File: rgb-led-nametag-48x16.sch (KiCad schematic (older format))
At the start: 25 parts, among them J1 USB_C_Receptacle_USB2.0, J2 TagConnect_TC2030_SWD, U25 STM32F722RETx, U26 SRV05-4, U27 TPS63001

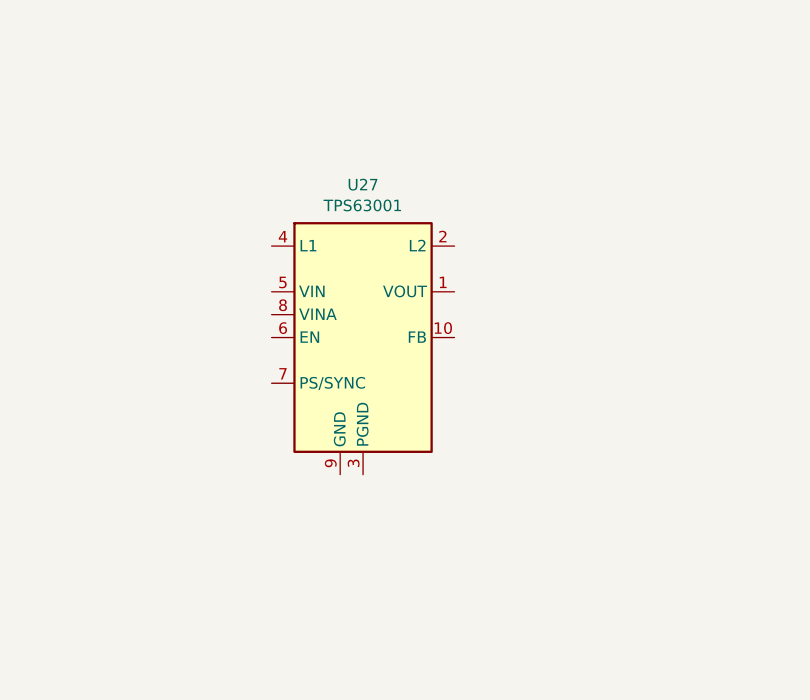
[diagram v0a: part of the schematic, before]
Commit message: Layout 3V3 buck/boost converter
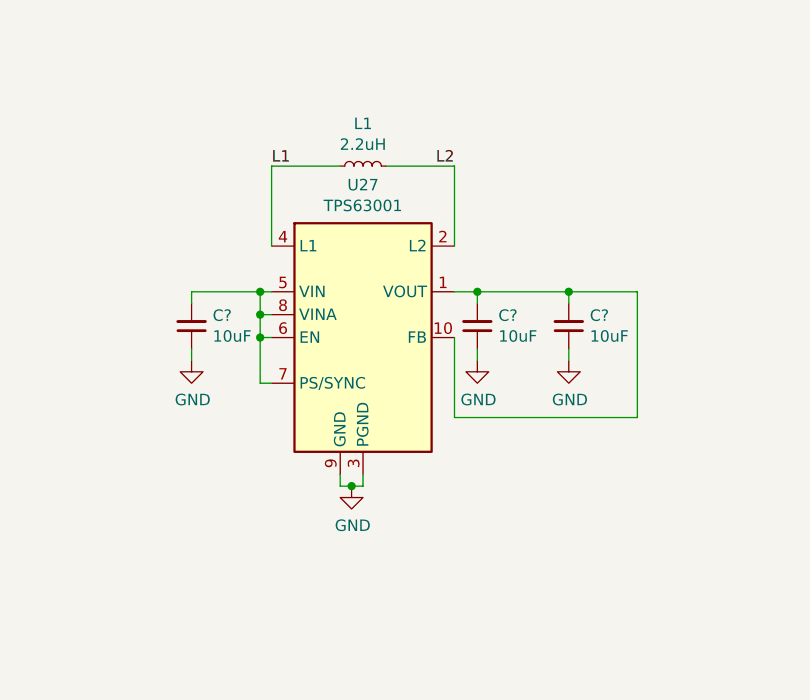
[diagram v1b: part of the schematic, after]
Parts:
- added C? (x3): 10uF, Capacitor_SMD:C_0402_1005Metric, symbol Device:C_Small
- added L1: 2.2uH, Inductor_SMD:L_Taiyo-Yuden_MD-3030, symbol Device:L_Small
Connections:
- net GND: now also U27.11 (PGND), U27.3 (PGND), U27.9 (GND), C?.1, C?.1, C?.1
- net at U27.1 (VOUT): now also U27.10 (FB), C?.2, C?.2
- net L2: now reaches U27.2 (L2)
- net L2: now also L1.2
- net L1: now reaches U27.4 (L1)
- net L1: now also L1.1
- net at U27.5 (VIN): now also U27.6 (EN), U27.7 (PS/SYNC), U27.8 (VINA), C?.2
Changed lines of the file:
@@
 	1550 4550 1550 4500
 Connection ~ 1550 4500
+$Comp
+L Device:L_Small L1
+U 1 1 623B26A7
+P 12600 1150
+F 0 "L1" V 12785 1150 50  0000 C CNN
+F 1 "2.2uH" V 12694 1150 50  0000 C CNN
+F 2 "Inductor_SMD:L_Taiyo-Yuden_MD-3030" H 12600 1150 50  0001 C CNN
+F 3 "~" H 12600 1150 50  0001 C CNN
+F 4 "C43389" V 12600 1150 50  0001 C CNN "LCSC"
+	1    12600 1150
+	0    -1   -1   0
+$EndComp
+Wire Wire Line
+	12500 1150 12200 1150
+Wire Wire Line
+	12200 1150 12200 1500
+Wire Wire Line
+	12700 1150 13000 1150
+Wire Wire Line
+	13000 1150 13000 1500
+Text Label 12200 1150 0    50   ~ 0
+L1
+Text Label 13000 1150 2    50   ~ 0
+L2
+$Comp
+L Device:C_Small C?
+U 1 1 623DDBAB
+P 11850 1850
+AR Path="/620161BA/623DDBAB" Ref="C?"  Part="1"
+AR Path="/623DDBAB" Ref="C?"  Part="1"
+F 0 "C?" H 11758 1804 50  0000 R CNN
+F 1 "10uF" H 11758 1895 50  0000 R CNN
+F 2 "Capacitor_SMD:C_0402_1005Metric" H 11850 1850 50  0001 C CNN
+F 3 "~" H 11850 1850 50  0001 C CNN
+F 4 "C15525" H 11850 1850 50  0001 C CNN "LCSC"
+	1    11850 1850
+	-1   0    0    1
+$EndComp
+Wire Wire Line
+	12200 1700 12150 1700
+Wire Wire Line
+	11850 1700 11850 1750
+Wire Wire Line
+	12200 1800 12150 1800
+Wire Wire Line
+	12150 1800 12150 1700
+Connection ~ 12150 1700
+Wire Wire Line
+	12150 1700 11850 1700
+Wire Wire Line
+	12200 1900 12150 1900
+Wire Wire Line
+	12150 1900 12150 1800
+Connection ~ 12150 1800
+Wire Wire Line
+	12200 2100 12150 2100
+Wire Wire Line
+	12150 2100 12150 1900
+Connection ~ 12150 1900
+$Comp
+L power:GND #PWR?
+U 1 1 6241DC69
+P 11850 2000
+F 0 "#PWR?" H 11850 1750 50  0001 C CNN
+F 1 "GND" H 11855 1827 50  0000 C CNN
+F 2 "" H 11850 2000 50  0001 C CNN
+F 3 "" H 11850 2000 50  0001 C CNN
+	1    11850 2000
+	1    0    0    -1
+$EndComp
+Wire Wire Line
+	11850 2000 11850 1950
+$Comp
+L power:GND #PWR?
+U 1 1 6242BAF6
+P 12550 2550
+F 0 "#PWR?" H 12550 2300 50  0001 C CNN
+F 1 "GND" H 12555 2377 50  0000 C CNN
+F 2 "" H 12550 2550 50  0001 C CNN
+F 3 "" H 12550 2550 50  0001 C CNN
+	1    12550 2550
+	1    0    0    -1
+$EndComp
+Wire Wire Line
+	12500 2500 12500 2550
+Wire Wire Line
+	12500 2550 12550 2550
+Wire Wire Line
+	12600 2500 12600 2550
+Wire Wire Line
+	12600 2550 12550 2550
+Connection ~ 12550 2550
+$Comp
+L Device:C_Small C?
+U 1 1 62448BCD
+P 13100 1850
+AR Path="/620161BA/62448BCD" Ref="C?"  Part="1"
+AR Path="/62448BCD" Ref="C?"  Part="1"
+F 0 "C?" H 13008 1804 50  0000 R CNN
+F 1 "10uF" H 13008 1895 50  0000 R CNN
+F 2 "Capacitor_SMD:C_0402_1005Metric" H 13100 1850 50  0001 C CNN
+F 3 "~" H 13100 1850 50  0001 C CNN
+F 4 "C15525" H 13100 1850 50  0001 C CNN "LCSC"
+	1    13100 1850
+	-1   0    0    1
+$EndComp
+$Comp
+L Device:C_Small C?
+U 1 1 6245675E
+P 13500 1850
+AR Path="/620161BA/6245675E" Ref="C?"  Part="1"
+AR Path="/6245675E" Ref="C?"  Part="1"
+F 0 "C?" H 13408 1804 50  0000 R CNN
+F 1 "10uF" H 13408 1895 50  0000 R CNN
+F 2 "Capacitor_SMD:C_0402_1005Metric" H 13500 1850 50  0001 C CNN
+F 3 "~" H 13500 1850 50  0001 C CNN
+F 4 "C15525" H 13500 1850 50  0001 C CNN "LCSC"
+	1    13500 1850
+	-1   0    0    1
+$EndComp
+Wire Wire Line
+	13000 1700 13100 1700
+Wire Wire Line
+	13500 1700 13500 1750
+Wire Wire Line
+	13100 1750 13100 1700
+Connection ~ 13100 1700
+Wire Wire Line
+	13100 1700 13500 1700
+$Comp
+L power:GND #PWR?
+U 1 1 6247F801
+P 13100 2000
+F 0 "#PWR?" H 13100 1750 50  0001 C CNN
+F 1 "GND" H 13105 1827 50  0000 C CNN
+F 2 "" H 13100 2000 50  0001 C CNN
+F 3 "" H 13100 2000 50  0001 C CNN
+	1    13100 2000
+	1    0    0    -1
+$EndComp
+Wire Wire Line
+	13100 2000 13100 1950
+$Comp
+L power:GND #PWR?
+U 1 1 6248E1C3
+P 13500 2000
+F 0 "#PWR?" H 13500 1750 50  0001 C CNN
+F 1 "GND" H 13505 1827 50  0000 C CNN
+F 2 "" H 13500 2000 50  0001 C CNN
+F 3 "" H 13500 2000 50  0001 C CNN
+	1    13500 2000
+	1    0    0    -1
+$EndComp
+Wire Wire Line
+	13500 2000 13500 1950
+Wire Wire Line
+	13000 1900 13000 2250
+Wire Wire Line
+	13000 2250 13800 2250
+Wire Wire Line
+	13800 2250 13800 1700
+Wire Wire Line
+	13800 1700 13500 1700
 Wire Bus Line
 	2950 1250 2950 6650
+Connection ~ 13500 1700
 $EndSCHEMATC

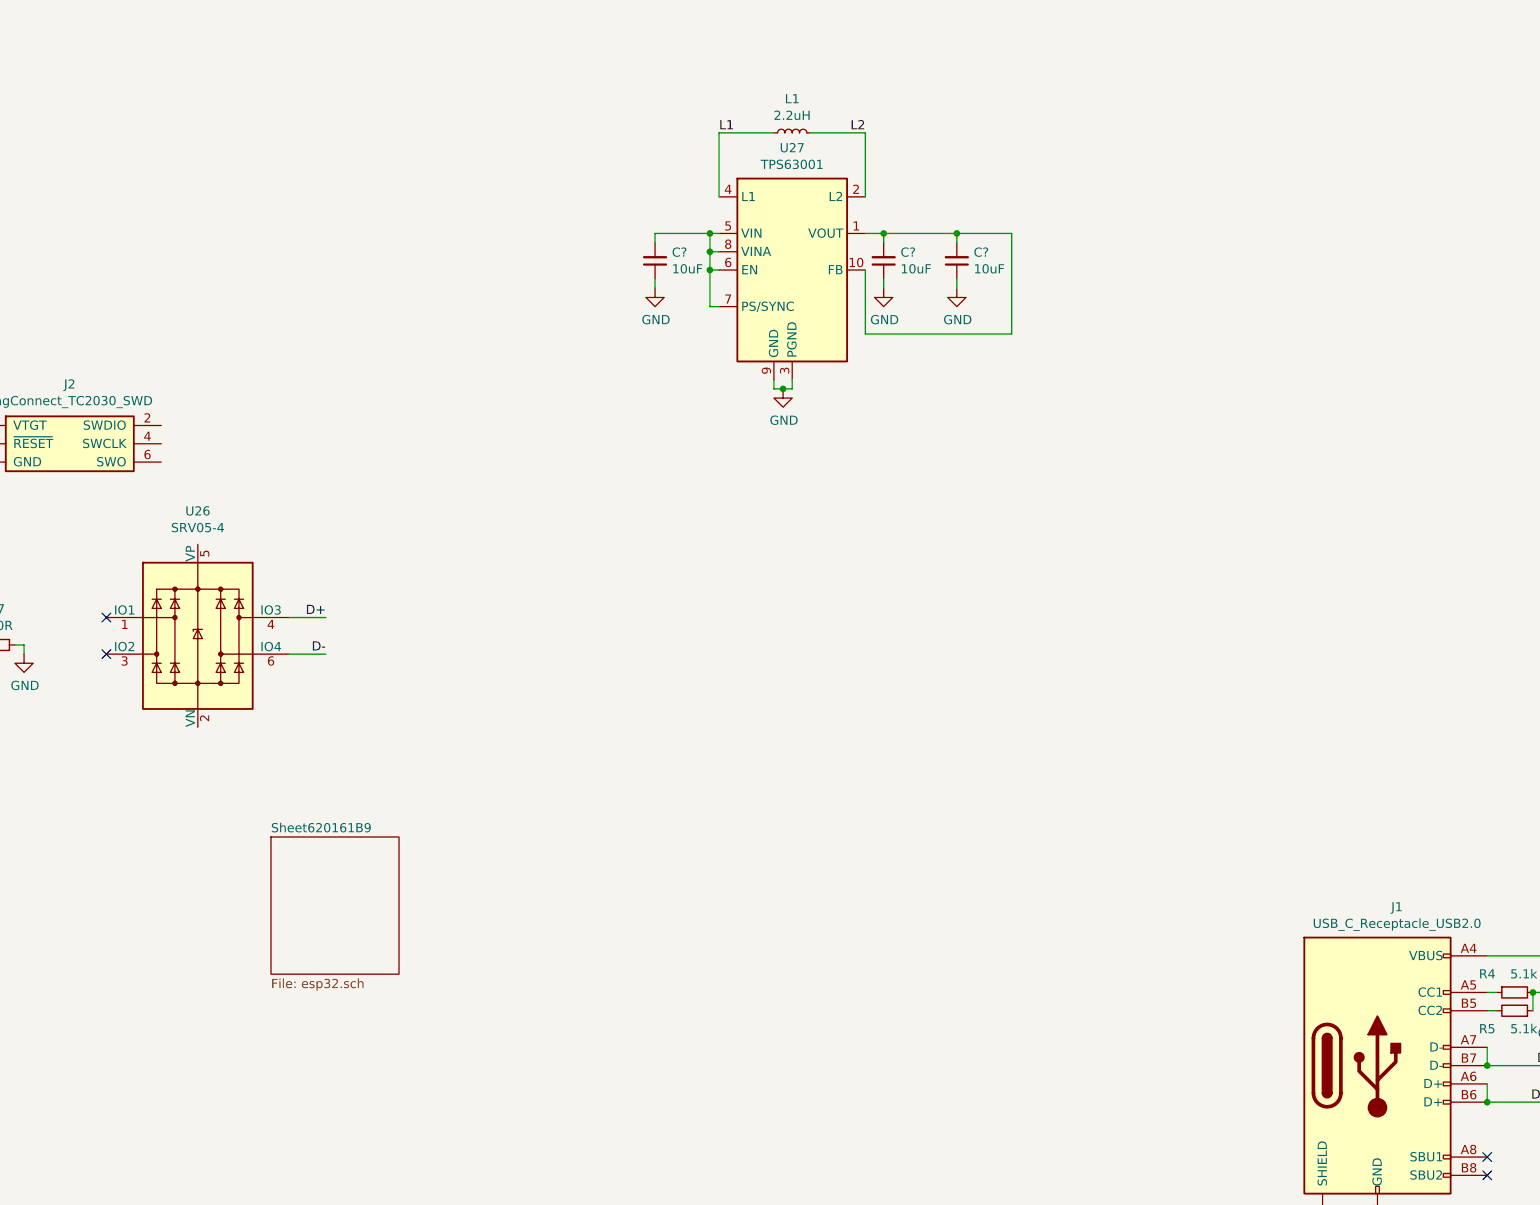
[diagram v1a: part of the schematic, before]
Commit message: Implement power path
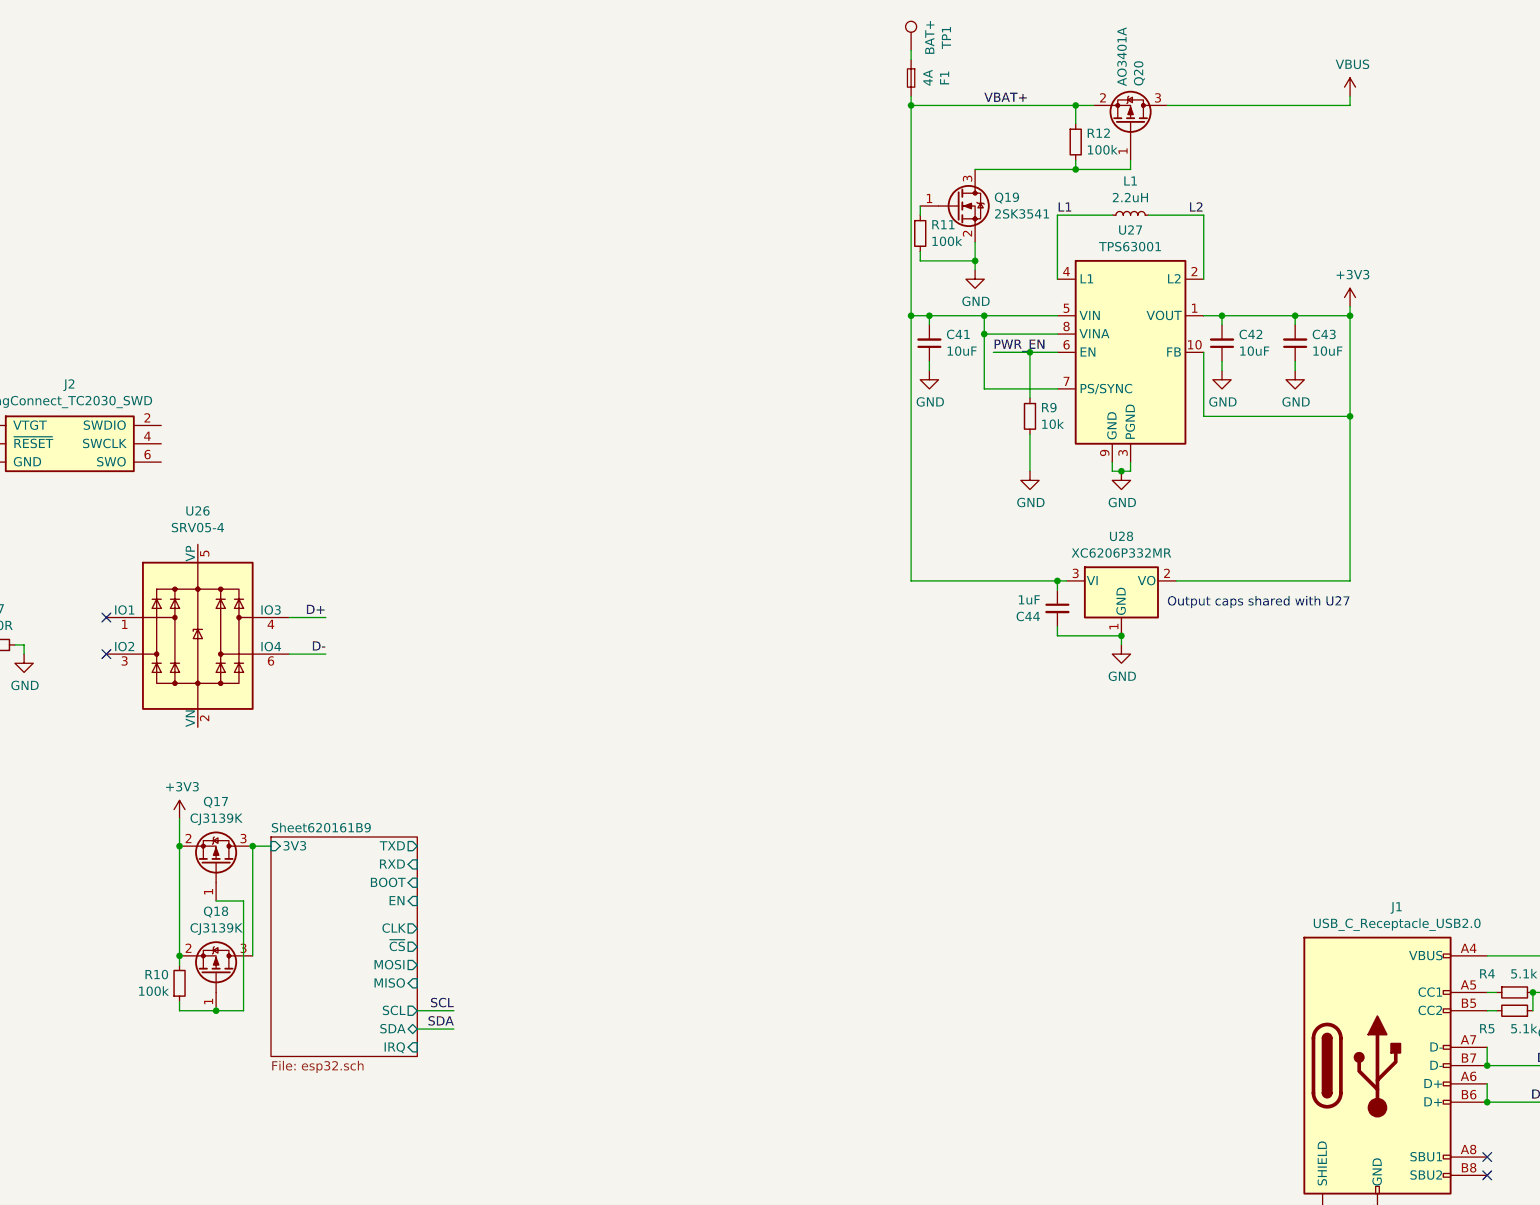
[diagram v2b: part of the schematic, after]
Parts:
- added C44: 1uF, Capacitor_SMD:C_0402_1005Metric, symbol Device:C_Small
- added F1: 4A, Resistor_SMD:R_0603_1608Metric, symbol Device:Fuse_Small
- added Q17, Q18: CJ3139K, Package_TO_SOT_SMD:SOT-723, symbol Transistor_FET:BSS84
- added Q19: 2SK3541, Package_TO_SOT_SMD:SOT-723, symbol Transistor_FET:2N7002
- added Q20: AO3401A, Package_TO_SOT_SMD:SOT-23, symbol Transistor_FET:AO3401A
- added R10, R11, R12: 100k, Resistor_SMD:R_0402_1005Metric, symbol Device:R_Small
- added R9: 10k, Resistor_SMD:R_0402_1005Metric, symbol Device:R_Small
- added TP1: BAT+, TestPoint:TestPoint_Pad_2.0x2.0mm, symbol Connector:TestPoint
- added U28: XC6206P332MR, Package_TO_SOT_SMD:SOT-23, symbol Regulator_Linear:XC6206PxxxMR
- U27: LCSC (none) -> C28060
- gave numbers to parts that had none: 3
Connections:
- net +3V3: now also C42.2, C43.2, U27.1 (VOUT), U27.10 (FB), Q17.2 (S), Q18.2 (S), R10.2, U28.2 (VO)
- net GND: now also C44.2, Q19.2 (S), R11.2, R9.2, U28.1 (GND)
- net VBUS: now also Q20.3 (D)
- net VBAT+: now reaches C41.2, U27.5 (VIN), U27.7 (PS/SYNC), U27.8 (VINA)
- net VBAT+: now also C44.1, F1.2, Q20.2 (S), R12.1, U28.3 (VI); no longer U27.6 (EN)
- new net: Q17.1 (G), Q18.1 (G), R10.1
- new net: Q19.3 (D), Q20.1 (G), R12.2
- new net: Q19.1 (G), R11.1
- new net: F1.1, TP1.1
- new net PWR_EN: R9.1, U27.6 (EN)
- new net Sheet620161B9/3V3: Q17.3 (D), Q18.3 (D)
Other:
- note added: "Output caps shared with U27"
- moved on the sheet: C41, C42, C43, L1, U27
